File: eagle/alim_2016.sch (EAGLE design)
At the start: 46 parts, among them J1 AVR_SPI_PRG_6PTH, J2 AVR_SPI_PRG_6PTH, U1 3.3V, U2 LM2678S-5.0, U4 LM2596S-ADJ, U5 ATTINY85-20SU, U6 ATMEGA328P_TQFP

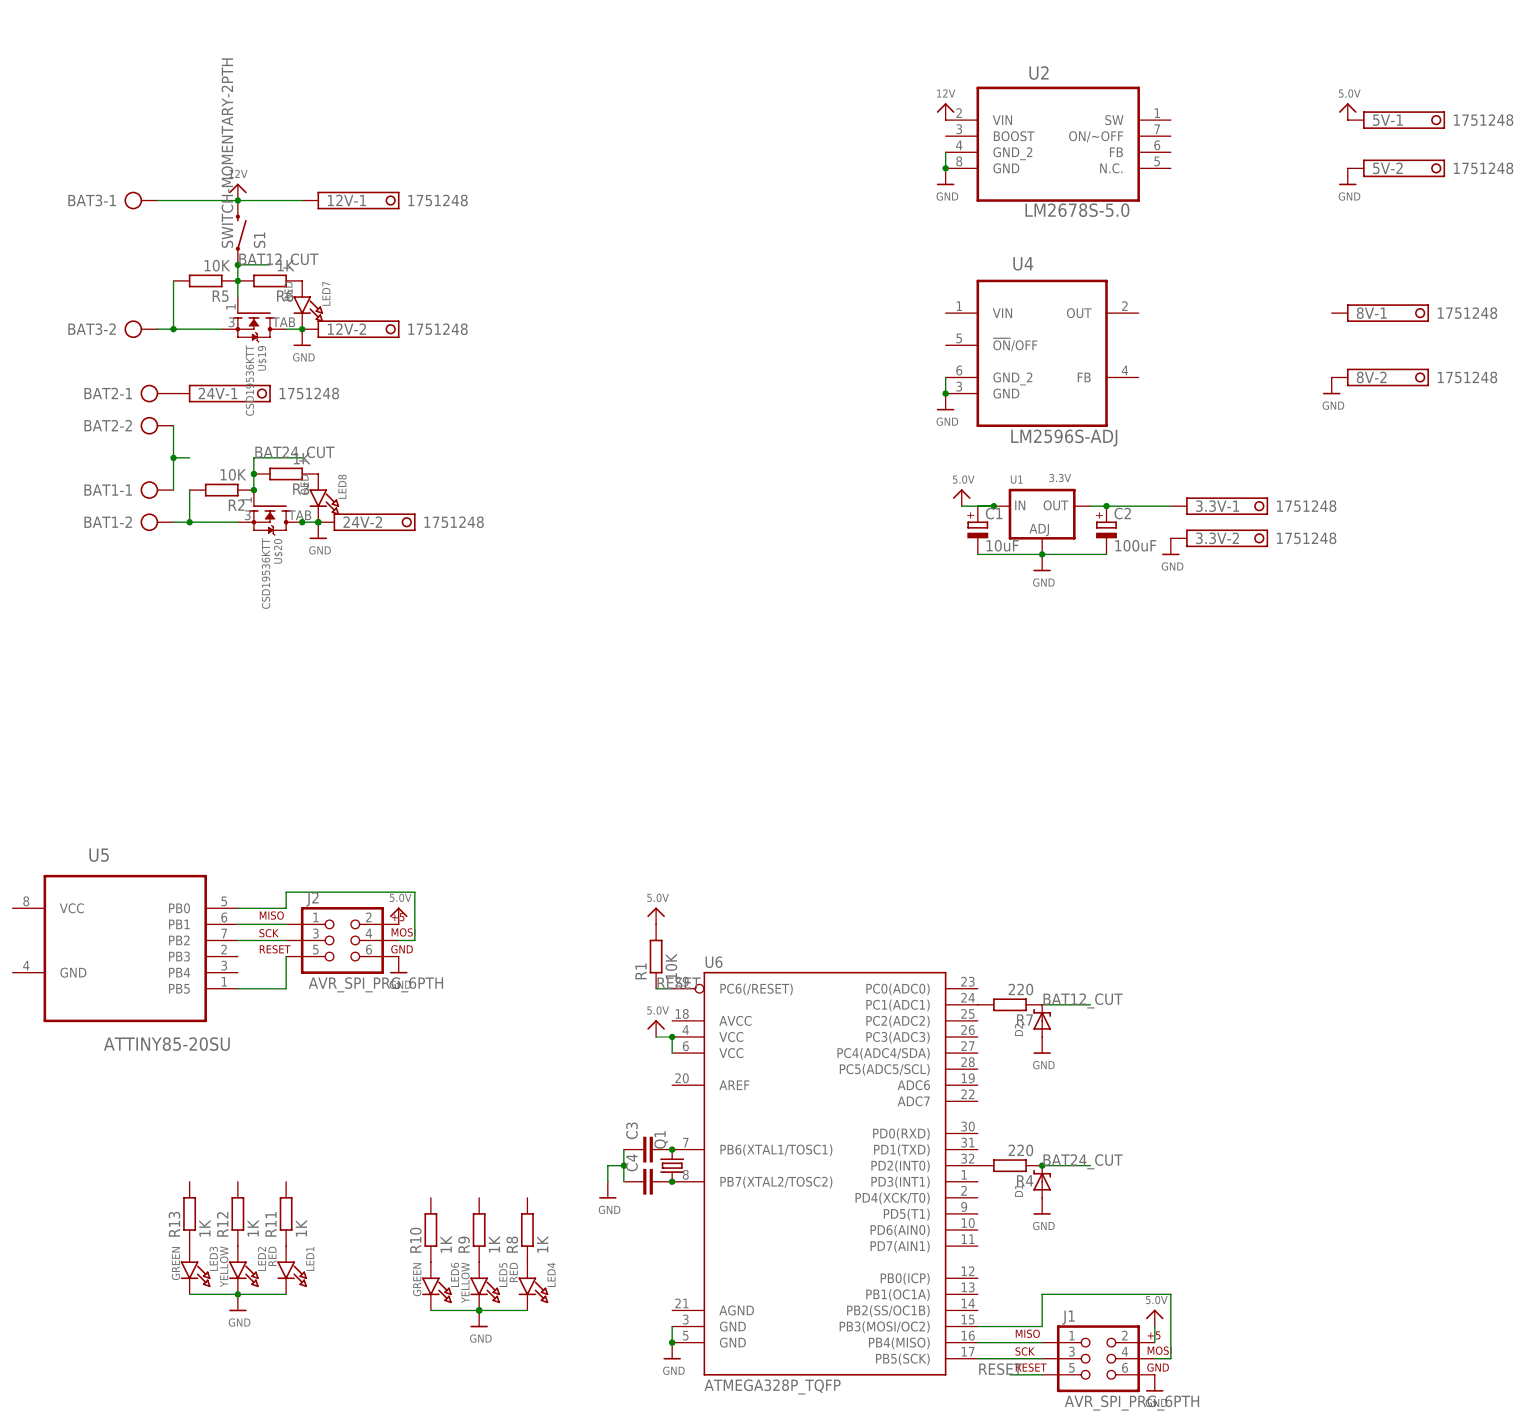
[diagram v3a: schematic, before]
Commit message: adding battery voltage sense
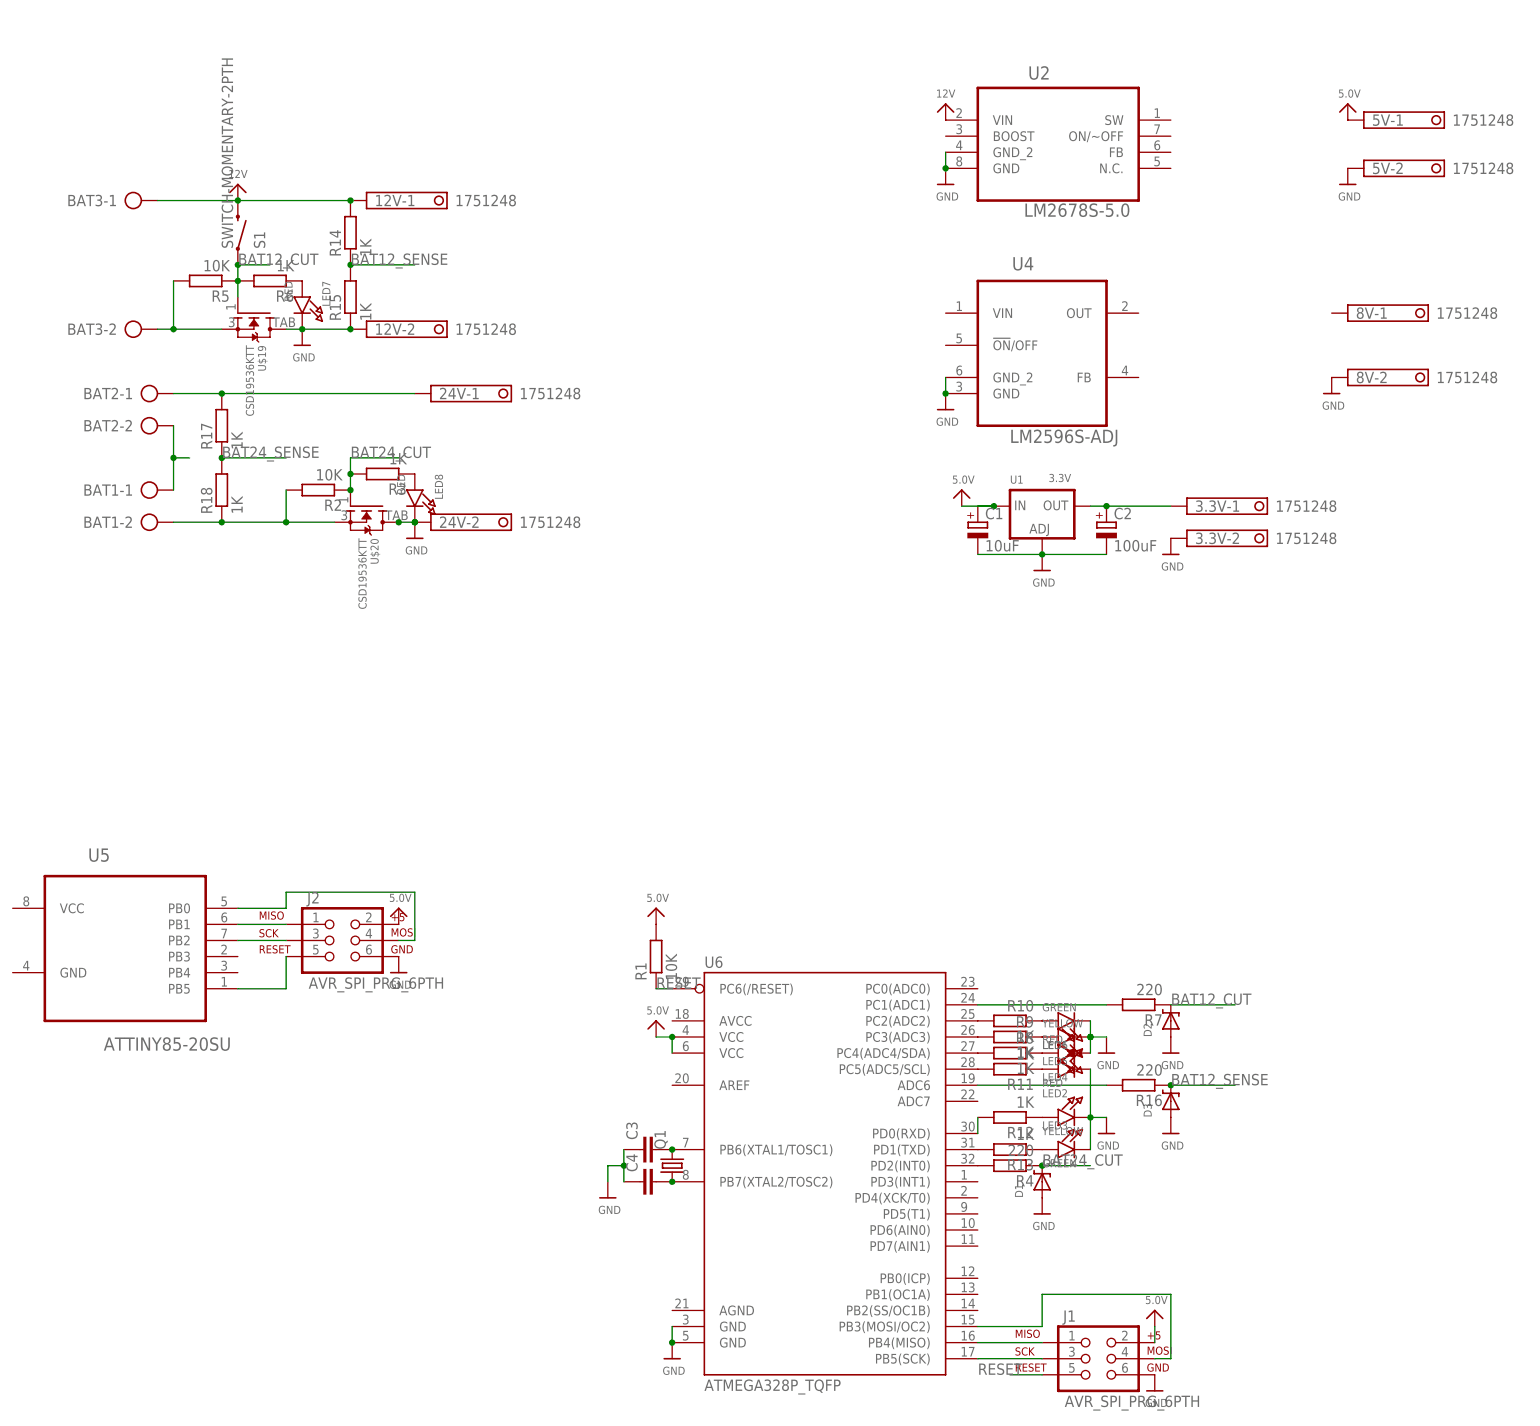
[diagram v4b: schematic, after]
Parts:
- added D3: (no value), alim:DIODE-ZENERSOD123
- added R14, R15, R17, R18: 1K, resistor:R-EU_M0805
- added R16: 220, resistor:R-EU_M0805
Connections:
- new net BAT12_SENSE: D3.C, R14.1, R15.2, R16.1
- new net BAT24_SENSE: R17.1, R18.2
- new net N$21: R10.2, U6.PC2(ADC2)
- new net N$22: R9.2, U6.PC3(ADC3)
- new net N$23: R8.2, U6.PC4(ADC4/SDA)
- new net N$24: R13.2, U6.PD1(TXD)
- new net N$25: R12.2, U6.PD0(RXD)
- new net N$26: R11.2, U6.PC5(ADC5/SCL)
- new net N$27: R16.2, U6.ADC6
- net 12V: now also R14.2
- net GND: now also D3.A, R15.1
- net N$12: now also R17.2
- net N$8: now also R18.1
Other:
- moved on the sheet: 12V-1, 12V-2, 24V-1, 24V-2, D2, LED1, LED2, LED3, LED4, LED5, LED6, LED8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
